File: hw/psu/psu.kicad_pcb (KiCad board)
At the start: 2 copper layers, 81 x 60 mm, 108 parts, among them J1 BATTERY, J2 CAN, J3 DEBUG, J4 SWD, J5 SDU, J6 HMI, J7 ECU, U1 INA180A1, U2 MCP2562-E-SN, U3 TS1117BCW33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

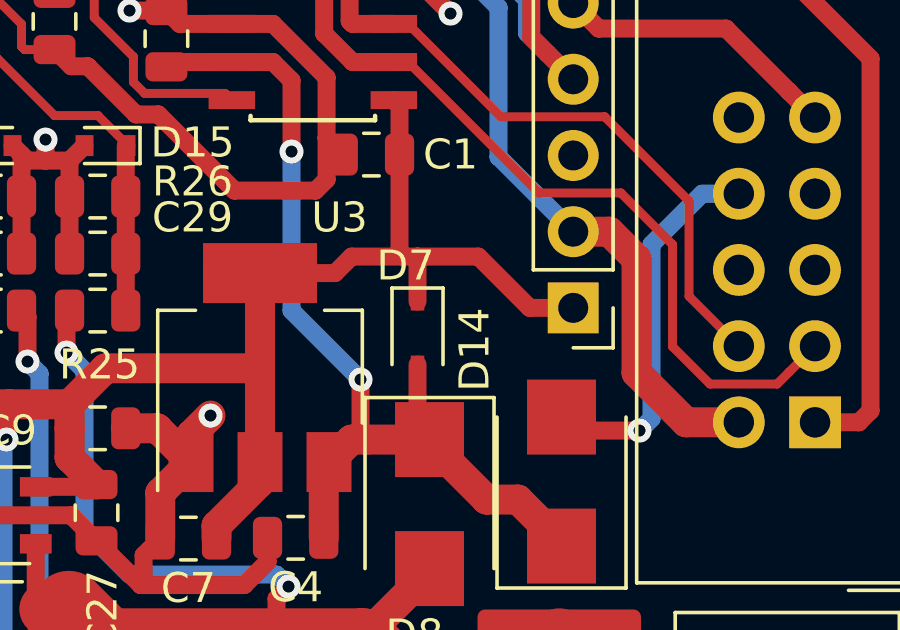
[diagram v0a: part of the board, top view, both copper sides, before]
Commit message: Fixed diode polarity
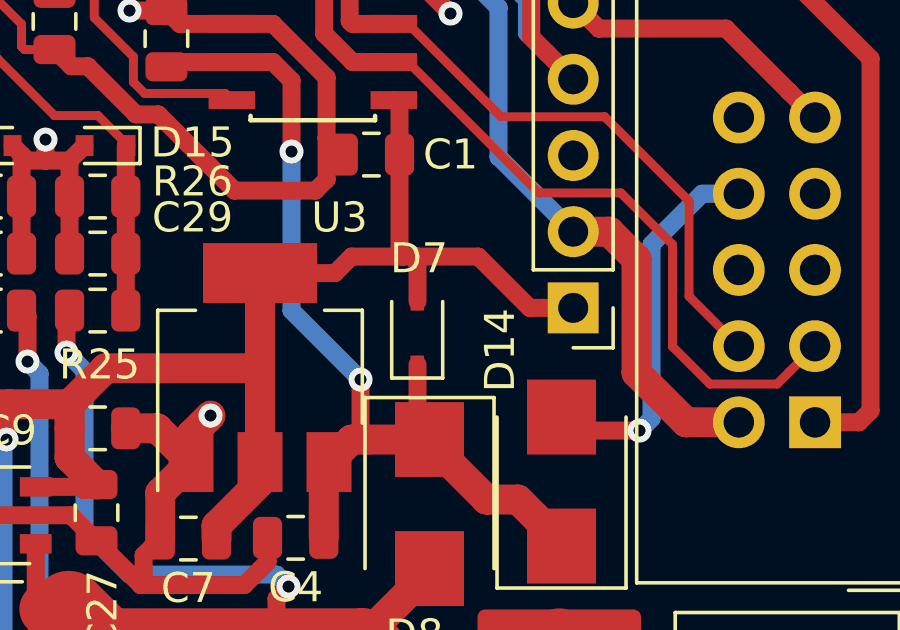
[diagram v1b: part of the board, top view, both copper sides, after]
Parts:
- turned D7 to 90 degrees
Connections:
- D7 pad 1: +3V3 -> +5VA
- D7 pad 2: +5VA -> +3V3
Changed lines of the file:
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@@
   )
   (module Diode_SMD:D_SOD-323 (layer F.Cu)
-    (at 189.1 79.95 270)
+    (at 189.09 79.95 90)
     (descr SOD-323)
     (tags SOD-323)
     (attr smd)
-    (fp_text reference D7 (at -2.25 0.4) (layer F.SilkS)
-      (effects (font (size 1 1) (thickness 0.15)))
-    )
-    (fp_text value BAT60 (at 0.1 1.9 270) (layer F.Fab)
-      (effects (font (size 1 1) (thickness 0.15)))
-    )
-    (fp_text user %R (at 0 -1.85 270) (layer F.Fab)
+    (fp_text reference D7 (at 2.49 0.06 -180) (layer F.SilkS)
+      (effects (font (size 1 1) (thickness 0.15)))
+    )
+    (fp_text value BAT60 (at 0.1 1.9 90) (layer F.Fab)
+      (effects (font (size 1 1) (thickness 0.15)))
+    )
+    (fp_text user %R (at 0 -1.85 90) (layer F.Fab)
       (effects (font (size 1 1) (thickness 0.15)))
     )
@@
     (fp_line (start -1.5 0.85) (end 1.05 0.85) (layer F.SilkS) (width 0.12))
     (fp_line (start -1.5 -0.85) (end 1.05 -0.85) (layer F.SilkS) (width 0.12))
-    (pad 1 smd rect (at -1.05 0 270) (size 0.6 0.45) (layers F.Cu F.Paste F.Mask)
+    (pad 1 smd rect (at -1.05 0 90) (size 0.6 0.45) (layers F.Cu F.Paste F.Mask)
+      (net 3 +5VA))
+    (pad 2 smd rect (at 1.05 0 90) (size 0.6 0.45) (layers F.Cu F.Paste F.Mask)
       (net 1 +3V3))
-    (pad 2 smd rect (at 1.05 0 270) (size 0.6 0.45) (layers F.Cu F.Paste F.Mask)
-      (net 3 +5VA))
     (model ${KISYS3DMOD}/Diode_SMD.3dshapes/D_SOD-323.wrl
       (at (xyz 0 0 0))
@@
     (tags "Diode SMB (DO-214AA)")
     (attr smd)
-    (fp_text reference D14 (at -5.15 -1.5 270) (layer F.SilkS)
-      (effects (font (size 1 1) (thickness 0.15)))
-    )
+    (fp_text reference D14 (at -5.13 -2.35 90) (layer F.SilkS)
+      (effects (font (size 1 1) (thickness 0.15)))
+    )
